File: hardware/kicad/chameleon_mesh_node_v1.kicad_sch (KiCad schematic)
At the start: 6 parts, among them J1 USB-C Power+Data, J2 LiPo JST (PH 2.0), U1 BQ24074RGT, U2 XIAO-ESP32-C5-SMD, U3 Wio-WM1110, U4 BME280

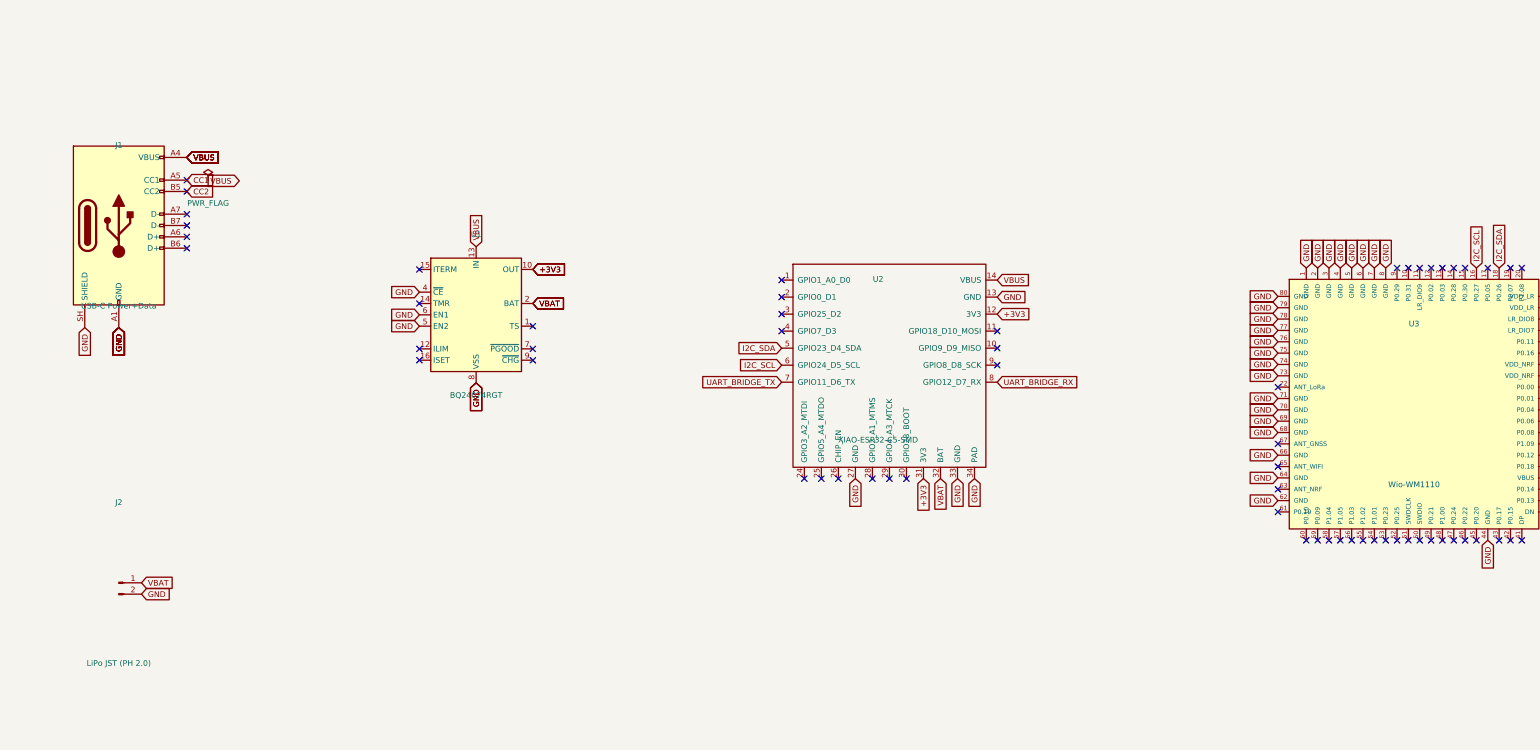
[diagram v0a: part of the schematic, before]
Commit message: hardware: v1.2 USB-flush board — replace v1.1, add BME280 decoupling
v1.2 fixes the USB-C-can't-seat defect: the top edge is truncated 60x40 -> 60x34
so the connector mouth is flush with the board edge. The DNP BQ24074 charger (U1)
and the LiPo connector (J2) are removed (their dead VBAT traces shorted the
relocated mounting hole), so the board is USB-powered only. Mounting holes moved
into the new outline.

- Added C1, a 100nF 0402 decoupling cap at the BME280 VDD (placed + routed to
  +3V3, GND via the ground pour).
- Schematic reconciled to the board (U1/J2 + battery nets removed); ERC 0/0.
  The schematic is a system block diagram; board-level passives (C1) are carried
  in the BOM, placement, and gerbers.
- BOM, pick-and-place, renders, and gerbers regenerated; PCB DRC 0 errors,
  0 unconnected nets.
- Docs corrected to v1.2: dimensions, USB-only power tree, DRC counts, routing
  description. fp-lib-table reduced to the project's own custom libraries.
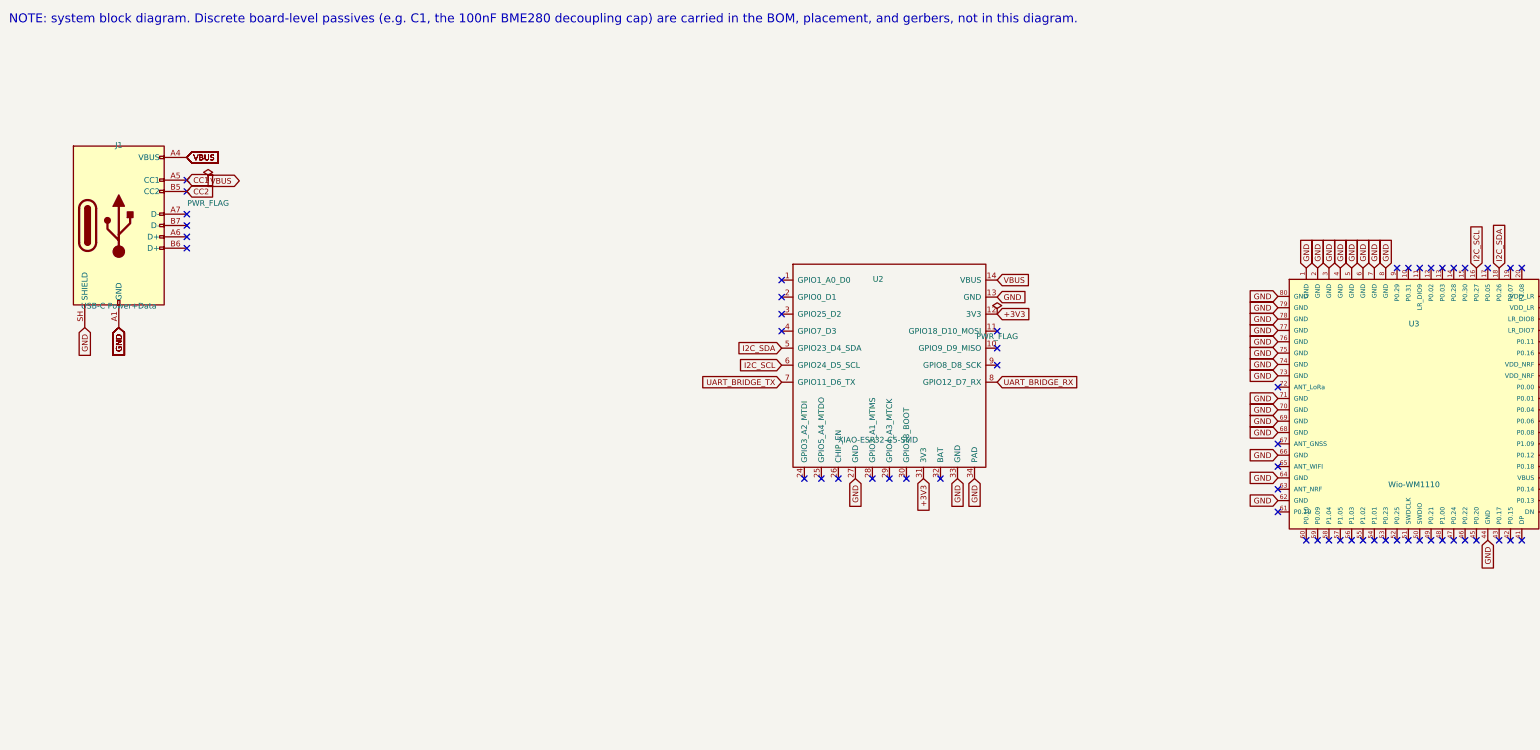
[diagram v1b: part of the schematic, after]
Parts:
- removed J2: LiPo JST (PH 2.0), Connector_JST:JST_PH_S2B-PH-K_1x02_P2.00mm_Horizontal, symbol Connector:Conn_01x02_Pin
- removed U1: BQ24074RGT, Package_DFN_QFN:QFN-16-1EP_3x3mm_P0.5mm_EP1.675x1.675mm, symbol Battery_Management:BQ24074RGT
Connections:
- net VBAT: no longer names the net of U2.32 (BAT)
- no-connect marks 74 -> 68
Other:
- note added: "NOTE: system block diagram. Discrete board-level passives (e.g. C1, the 100nF BME280 decoupling cap) are carried in the BOM, placement, and gerbers, not in this diagram."
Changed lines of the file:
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@@
 (kicad_sch
 	(version 20240329)
-	(generator "kicad-python")
+	(generator "kicad")
 	(generator_version "10.0")
 	(paper "A3")
@@
 		(title "Chameleon Mesh Node v1")
 		(date "2026-05-16")
-		(rev "v1.0-DRAFT")
+		(rev "v1.2")
 		(company "Chameleon Mesh Node Project")
 		(comment 1 "Dual-radio telemetry motherboard")
-		(comment 2 "Seeed Meshtastic Build-Off entry — dual-radio mesh node")
+		(comment 2 "Seeed Meshtastic Build-Off entry / dual-radio")
 		(comment 3 "Wio-WM1110 + XIAO ESP32-C5 + BQ24074 + BME280")
 		(comment 4 "Logical net mapping; PCB routing deferred")
@@
 	)
 	(symbol
-		(lib_id "Battery_Management:BQ24074RGT")
-		(at 130.00 80.00 0)
-		(unit 1)
-		(exclude_from_sim no)
-		(in_bom yes)
-		(on_board yes)
-		(dnp no)
-		(property "Reference" "U1"
-			(at 130.00 62.00 0)
-			(effects (font (size 1.27 1.27)))
-		)
-		(property "Value" "BQ24074RGT"
-			(at 130.00 98.00 0)
-			(effects (font (size 1.27 1.27)))
-		)
-		(property "Footprint" "Package_DFN_QFN:QFN-16-1EP_3x3mm_P0.5mm_EP1.675x1.675mm"
-			(at 130.00 80.00 0)
-			(effects (font (size 1.27 1.27)) (hide yes))
-		)
-		(property "Datasheet" ""
-			(at 130.00 80.00 0)
-			(effects (font (size 1.27 1.27)) (hide yes))
-		)
-		(instances
-			(project ""
-				(path "/08bddda4-777a-4465-8af5-7e5907361ace"
-					(reference "U1") (unit 1)
-				)
-			)
-		)
-	)
-	(symbol
-		(lib_id "Connector:Conn_01x02_Pin")
-		(at 50.00 140.00 0)
-		(unit 1)
-		(exclude_from_sim no)
-		(in_bom yes)
-		(on_board yes)
-		(dnp no)
-		(property "Reference" "J2"
-			(at 50.00 122.00 0)
-			(effects (font (size 1.27 1.27)))
-		)
-		(property "Value" "LiPo JST (PH 2.0)"
-			(at 50.00 158.00 0)
-			(effects (font (size 1.27 1.27)))
-		)
-		(property "Footprint" "Connector_JST:JST_PH_S2B-PH-K_1x02_P2.00mm_Horizontal"
-			(at 50.00 140.00 0)
-			(effects (font (size 1.27 1.27)) (hide yes))
-		)
-		(property "Datasheet" ""
-			(at 50.00 140.00 0)
-			(effects (font (size 1.27 1.27)) (hide yes))
-		)
-		(instances
-			(project ""
-				(path "/08bddda4-777a-4465-8af5-7e5907361ace"
-					(reference "J2") (unit 1)
-				)
-			)
-		)
-	)
-	(symbol
 		(lib_id "Seeed_XIAO_Series:XIAO-ESP32-C5-SMD")
 		(at 220.00 90.00 0)
@@
 		(effects (font (size 1.27 1.27)))
 	)
+	(global_label "+3V3"
+		(shape input)
+		(at 246.67 79.84 0)
+		(effects (font (size 1.27 1.27)))
+	)
+	(global_label "+3V3"
+		(shape input)
+		(at 230.16 116.67 270)
+		(effects (font (size 1.27 1.27)))
+	)
+	(global_label "GND"
+		(shape input)
+		(at 246.67 76.03 0)
+		(effects (font (size 1.27 1.27)))
+	)
+	(global_label "GND"
+		(shape input)
+		(at 214.92 116.67 270)
+		(effects (font (size 1.27 1.27)))
+	)
+	(global_label "GND"
+		(shape input)
+		(at 237.78 116.67 270)
+		(effects (font (size 1.27 1.27)))
+	)
+	(global_label "GND"
+		(shape input)
+		(at 241.59 116.67 270)
+		(effects (font (size 1.27 1.27)))
+	)
 	(global_label "VBUS"
 		(shape input)
-		(at 130.00 64.76 90)
-		(effects (font (size 1.27 1.27)))
-	)
-	(global_label "GND"
-		(shape input)
-		(at 130.00 95.24 270)
-		(effects (font (size 1.27 1.27)))
-	)
-	(global_label "GND"
-		(shape input)
-		(at 130.00 95.24 270)
-		(effects (font (size 1.27 1.27)))
-	)
-	(global_label "VBAT"
-		(shape input)
-		(at 142.70 77.46 0)
-		(effects (font (size 1.27 1.27)))
-	)
-	(global_label "VBAT"
-		(shape input)
-		(at 142.70 77.46 0)
-		(effects (font (size 1.27 1.27)))
-	)
-	(global_label "+3V3"
-		(shape input)
-		(at 142.70 69.84 0)
-		(effects (font (size 1.27 1.27)))
-	)
-	(global_label "+3V3"
-		(shape input)
-		(at 142.70 69.84 0)
-		(effects (font (size 1.27 1.27)))
-	)
-	(global_label "GND"
-		(shape input)
-		(at 117.30 74.92 180)
-		(effects (font (size 1.27 1.27)))
-	)
-	(global_label "GND"
-		(shape input)
-		(at 117.30 82.54 180)
-		(effects (font (size 1.27 1.27)))
-	)
-	(global_label "GND"
-		(shape input)
-		(at 117.30 80.00 180)
-		(effects (font (size 1.27 1.27)))
-	)
-	(global_label "VBAT"
-		(shape input)
-		(at 55.08 140.00 0)
-		(effects (font (size 1.27 1.27)))
-	)
-	(global_label "GND"
-		(shape input)
-		(at 55.08 142.54 0)
-		(effects (font (size 1.27 1.27)))
-	)
-	(global_label "+3V3"
-		(shape input)
-		(at 246.67 79.84 0)
-		(effects (font (size 1.27 1.27)))
-	)
-	(global_label "+3V3"
-		(shape input)
-		(at 230.16 116.67 270)
-		(effects (font (size 1.27 1.27)))
-	)
-	(global_label "GND"
-		(shape input)
-		(at 246.67 76.03 0)
-		(effects (font (size 1.27 1.27)))
-	)
-	(global_label "GND"
-		(shape input)
-		(at 214.92 116.67 270)
-		(effects (font (size 1.27 1.27)))
-	)
-	(global_label "GND"
-		(shape input)
-		(at 237.78 116.67 270)
-		(effects (font (size 1.27 1.27)))
-	)
-	(global_label "GND"
-		(shape input)
-		(at 241.59 116.67 270)
-		(effects (font (size 1.27 1.27)))
-	)
-	(global_label "VBUS"
-		(shape input)
 		(at 246.67 72.22 0)
-		(effects (font (size 1.27 1.27)))
-	)
-	(global_label "VBAT"
-		(shape input)
-		(at 233.97 116.67 270)
 		(effects (font (size 1.27 1.27)))
 	)
@@
 	(no_connect (at 65.24 49.84))
 	(no_connect (at 65.24 52.38))
-	(no_connect (at 142.70 82.54))
-	(no_connect (at 142.70 87.62))
-	(no_connect (at 142.70 90.16))
-	(no_connect (at 117.30 87.62))
-	(no_connect (at 117.30 77.46))
-	(no_connect (at 117.30 69.84))
-	(no_connect (at 117.30 90.16))
 	(no_connect (at 198.41 72.22))
 	(no_connect (at 198.41 76.03))
@@
 	(no_connect (at 309.52 108.89))
 	(no_connect (at 309.52 96.19))
+	(no_connect (at 233.97 116.67))
+	(symbol
+		(lib_id "power:PWR_FLAG")
+		(at 246.67 79.84 0)
+		(unit 1)
+		(exclude_from_sim no)
+		(in_bom yes)
+		(on_board yes)
+		(dnp no)
+		(property "Reference" "#FLG3V3"
+			(at 246.67 74.84 0)
+			(effects (font (size 1.27 1.27)) (hide yes))
+		)
+		(property "Value" "PWR_FLAG"
+			(at 246.67 84.84 0)
+			(effects (font (size 1.27 1.27)))
+		)
+		(property "Footprint" ""
+			(at 246.67 79.84 0)
+			(effects (font (size 1.27 1.27)) (hide yes))
+		)
+		(property "Datasheet" ""
+			(at 246.67 79.84 0)
+			(effects (font (size 1.27 1.27)) (hide yes))
+		)
+		(instances
+			(project ""
+				(path "/08bddda4-777a-4465-8af5-7e5907361ace"
+					(reference "#FLG3V3") (unit 1)
+				)
+			)
+		)
+	)
+	(text "NOTE: system block diagram. Discrete board-level passives (e.g. C1, the 100nF BME280 decoupling cap) are carried in the BOM, placement, and gerbers, not in this diagram."
+		(exclude_from_sim no)
+		(at 25.4 15.0 0)
+		(effects
+			(font (size 2 2))
+			(justify left bottom)
+		)
+	)
 	(sheet_instances
 		(path "/" (page "1"))
